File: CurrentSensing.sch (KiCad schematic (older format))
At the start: 2 parts

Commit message: 第１版回路図完成
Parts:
- gave numbers to parts that had none: 2
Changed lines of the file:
@@
 encoding utf-8
 Sheet 4 5
-Title ""
+Title "Current Sensing"
 Date ""
 Rev ""
@@
 $EndDescr
 $Comp
-L Sensor_Current:ACS712xLCTR-30A U?
+L Sensor_Current:ACS712xLCTR-30A U9
 U 1 1 5C78E0F4
 P 5300 3750
-F 0 "U?" H 4700 3150 50  0000 C CNN
+F 0 "U9" H 4700 3150 50  0000 C CNN
 F 1 "ACS712xLCTR-30A" H 4700 3300 50  0000 C CNN
 F 2 "Package_SO:SOIC-8_3.9x4.9mm_P1.27mm" H 5400 3400 50  0001 L CIN
@@
 Connection ~ 4800 3900
 $Comp
-L Device:C_Small C?
+L Device:C_Small C19
 U 1 1 5C78E2D4
 P 5800 4000
-F 0 "C?" H 5892 4046 50  0000 L CNN
+F 0 "C19" H 5892 4046 50  0000 L CNN
 F 1 "10n" H 5892 3955 50  0000 L CNN
 F 2 "" H 5800 4000 50  0001 C CNN
@@
 	5800 3850 5800 3900
 $Comp
-L power:GND #PWR?
+L power:GND #PWR050
 U 1 1 5C78E3C5
 P 5800 4250
-F 0 "#PWR?" H 5800 4000 50  0001 C CNN
+F 0 "#PWR050" H 5800 4000 50  0001 C CNN
 F 1 "GND" H 5805 4077 50  0000 C CNN
 F 2 "" H 5800 4250 50  0001 C CNN
@@
 	5800 4100 5800 4250
 $Comp
-L power:GND #PWR?
+L power:GND #PWR049
 U 1 1 5C78E479
 P 5300 4250
-F 0 "#PWR?" H 5300 4000 50  0001 C CNN
+F 0 "#PWR049" H 5300 4000 50  0001 C CNN
 F 1 "GND" H 5305 4077 50  0000 C CNN
 F 2 "" H 5300 4250 50  0001 C CNN
@@
 	5300 3250 5300 3350
 $Comp
-L power:+5V #PWR?
+L power:+5V #PWR048
 U 1 1 5C791F98
 P 5300 3250
-F 0 "#PWR?" H 5300 3100 50  0001 C CNN
+F 0 "#PWR048" H 5300 3100 50  0001 C CNN
 F 1 "+5V" H 5315 3423 50  0000 C CNN
 F 2 "" H 5300 3250 50  0001 C CNN

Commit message: フットプリント割り付け＆Netリスト出力
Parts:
- C19: footprint (none) -> Capacitors_SMD:C_0603_HandSoldering
- U9: footprint Package_SO:SOIC-8_3.9x4.9mm_P1.27mm -> Housings_SOIC:SOIC-8_3.9x4.9mm_Pitch1.27mm
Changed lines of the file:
@@
 F 0 "U9" H 4700 3150 50  0000 C CNN
 F 1 "ACS712xLCTR-30A" H 4700 3300 50  0000 C CNN
-F 2 "Package_SO:SOIC-8_3.9x4.9mm_P1.27mm" H 5400 3400 50  0001 L CIN
+F 2 "Housings_SOIC:SOIC-8_3.9x4.9mm_Pitch1.27mm" H 5400 3400 50  0001 L CIN
 F 3 "http://www.allegromicro.com/~/media/Files/Datasheets/ACS712-Datasheet.ashx?la=en" H 5300 3750 50  0001 C CNN
 	1    5300 3750
@@
 F 0 "C19" H 5892 4046 50  0000 L CNN
 F 1 "10n" H 5892 3955 50  0000 L CNN
-F 2 "" H 5800 4000 50  0001 C CNN
+F 2 "Capacitors_SMD:C_0603_HandSoldering" H 5800 4000 50  0001 C CNN
 F 3 "~" H 5800 4000 50  0001 C CNN
 	1    5800 4000

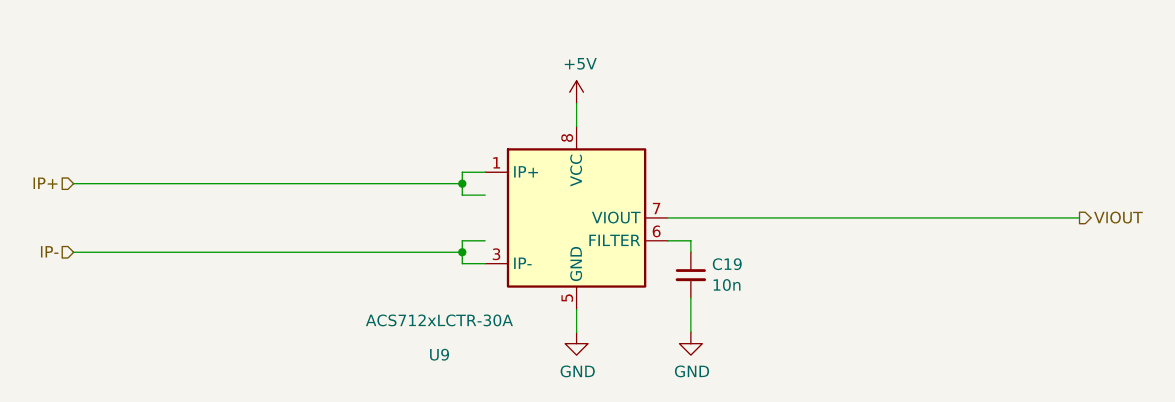
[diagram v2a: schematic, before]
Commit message: 電流センサ電源パスコン追加
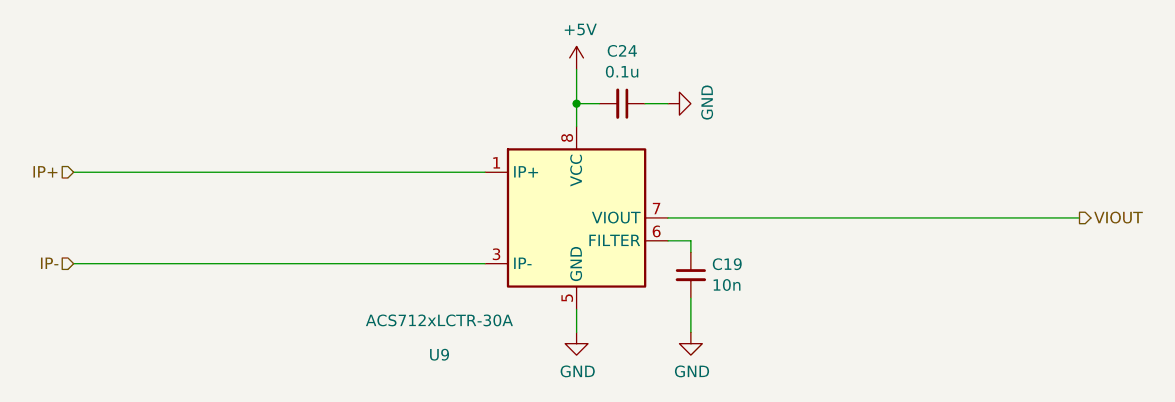
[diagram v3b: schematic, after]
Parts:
- added C24: 0.1u, Capacitors_SMD:C_0603_HandSoldering, symbol Device:C_Small
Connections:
- wire segments 16 -> 11
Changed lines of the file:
@@
 U 1 1 5C78E0F4
 P 5300 3750
+AR Path="/5C78E0F4" Ref="U9"  Part="1"
+AR Path="/5C77D686/5C78E0F4" Ref="U9"  Part="1"
 F 0 "U9" H 4700 3150 50  0000 C CNN
 F 1 "ACS712xLCTR-30A" H 4700 3300 50  0000 C CNN
@@
 	1    0    0    -1
 $EndComp
-Text HLabel 3100 3600 0    50   Input ~ 0
+Text HLabel 3100 3550 0    50   Input ~ 0
 IP+
-Text HLabel 3100 3900 0    50   Input ~ 0
+Text HLabel 3100 3950 0    50   Input ~ 0
 IP-
-Wire Wire Line
-	3100 3600 4800 3600
-Wire Wire Line
-	4800 3600 4800 3550
-Wire Wire Line
-	4800 3550 4900 3550
-Wire Wire Line
-	4800 3600 4800 3650
-Wire Wire Line
-	4800 3650 4900 3650
-Connection ~ 4800 3600
-Wire Wire Line
-	4900 3850 4800 3850
-Wire Wire Line
-	4800 3850 4800 3900
-Wire Wire Line
-	4800 3900 3100 3900
-Wire Wire Line
-	4800 3900 4800 3950
-Wire Wire Line
-	4800 3950 4900 3950
-Connection ~ 4800 3900
 $Comp
 L Device:C_Small C19
@@
 	7500 3750 5700 3750
 Wire Wire Line
-	5300 3250 5300 3350
+	5300 3100 5300 3250
 $Comp
 L power:+5V #PWR048
 U 1 1 5C791F98
-P 5300 3250
-F 0 "#PWR048" H 5300 3100 50  0001 C CNN
-F 1 "+5V" H 5315 3423 50  0000 C CNN
-F 2 "" H 5300 3250 50  0001 C CNN
-F 3 "" H 5300 3250 50  0001 C CNN
-	1    5300 3250
+P 5300 3100
+F 0 "#PWR048" H 5300 2950 50  0001 C CNN
+F 1 "+5V" H 5315 3273 50  0000 C CNN
+F 2 "" H 5300 3100 50  0001 C CNN
+F 3 "" H 5300 3100 50  0001 C CNN
+	1    5300 3100
 	1    0    0    -1
 $EndComp
+Wire Wire Line
+	3100 3550 4900 3550
+Wire Wire Line
+	3100 3950 4900 3950
+$Comp
+L Device:C_Small C24
+U 1 1 5C82A73B
+P 5500 3250
+F 0 "C24" V 5271 3250 50  0000 C CNN
+F 1 "0.1u" V 5362 3250 50  0000 C CNN
+F 2 "Capacitors_SMD:C_0603_HandSoldering" H 5500 3250 50  0001 C CNN
+F 3 "~" H 5500 3250 50  0001 C CNN
+	1    5500 3250
+	0    1    1    0
+$EndComp
+Wire Wire Line
+	5400 3250 5300 3250
+Connection ~ 5300 3250
+Wire Wire Line
+	5300 3250 5300 3350
+Wire Wire Line
+	5600 3250 5700 3250
+$Comp
+L power:GND #PWR0106
+U 1 1 5C82A868
+P 5700 3250
+F 0 "#PWR0106" H 5700 3000 50  0001 C CNN
+F 1 "GND" H 5705 3077 50  0000 C CNN
+F 2 "" H 5700 3250 50  0001 C CNN
+F 3 "" H 5700 3250 50  0001 C CNN
+	1    5700 3250
+	0    -1   -1   0
+$EndComp
 $EndSCHEMATC
